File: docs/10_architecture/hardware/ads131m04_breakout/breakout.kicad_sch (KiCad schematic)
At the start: 9 parts, among them J2 Data I/O, J3 Conn_01x10_Pin, U9 ADS131M04IPWR, Y1 CB3LV-3I-8M192000

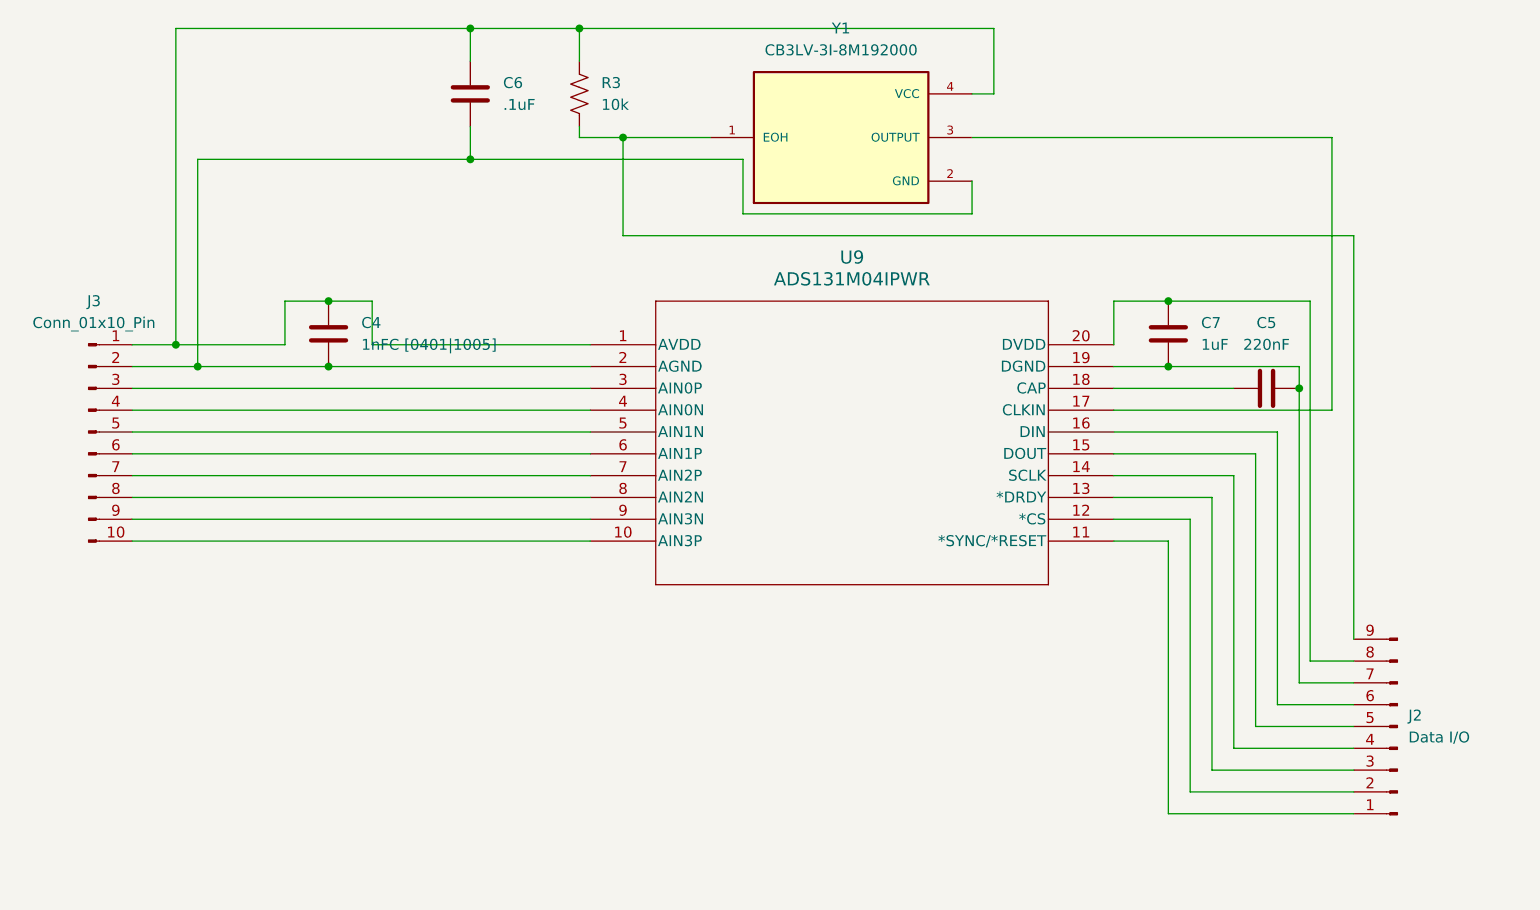
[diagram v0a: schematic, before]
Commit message: created ads131m04 breakout V1
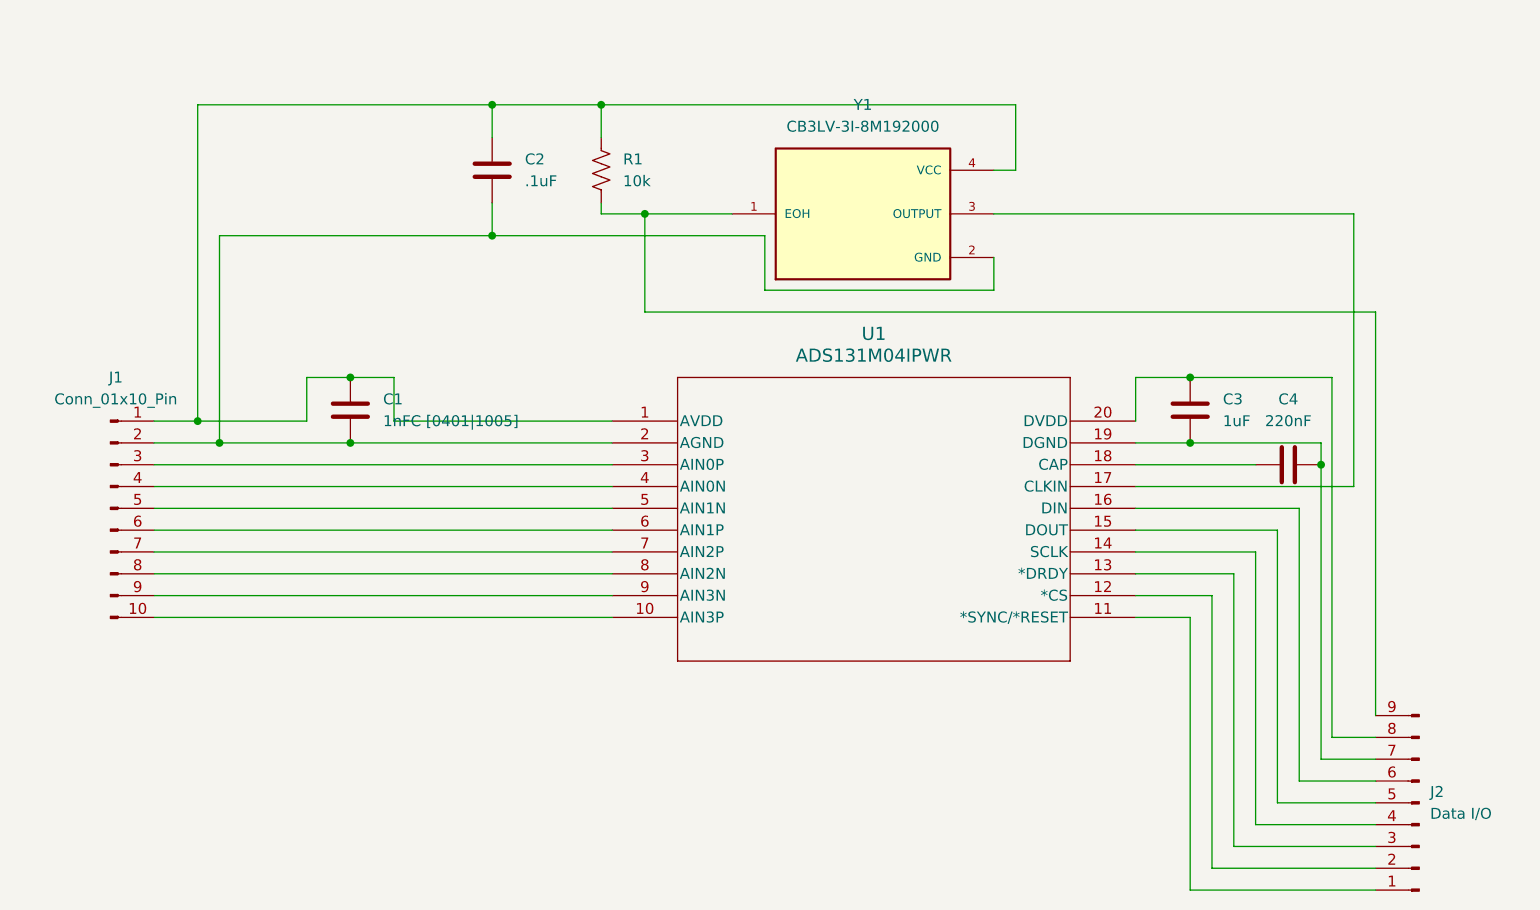
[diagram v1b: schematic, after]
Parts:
- C2: renamed from C6; footprint Capacitor_SMD:C_01005_0402Metric -> Capacitor_SMD:C_0201_0603Metric
- C3: renamed from C7; footprint Capacitor_SMD:C_01005_0402Metric -> Capacitor_SMD:C_0201_0603Metric
- J2: footprint (none) -> Connector_PinHeader_2.54mm:PinHeader_1x09_P2.54mm_Vertical
- U1: renamed from U9; footprint PW20_TEX -> Analog_DAC:PW20_TEX-L
- Y1: footprint CB3LV-3I-8M192000:OSC_CB3LV-3I-8M192000 -> Oscillator:OSC_CB3LV-3I-8M192000
- renumbered C4 to C1, C5 to C4, J3 to J1, R3 to R1
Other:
- moved on the sheet: C1, C2, C3, C4, J1, J2, R1, U1, Y1
